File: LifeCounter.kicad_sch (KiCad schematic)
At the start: 0 parts

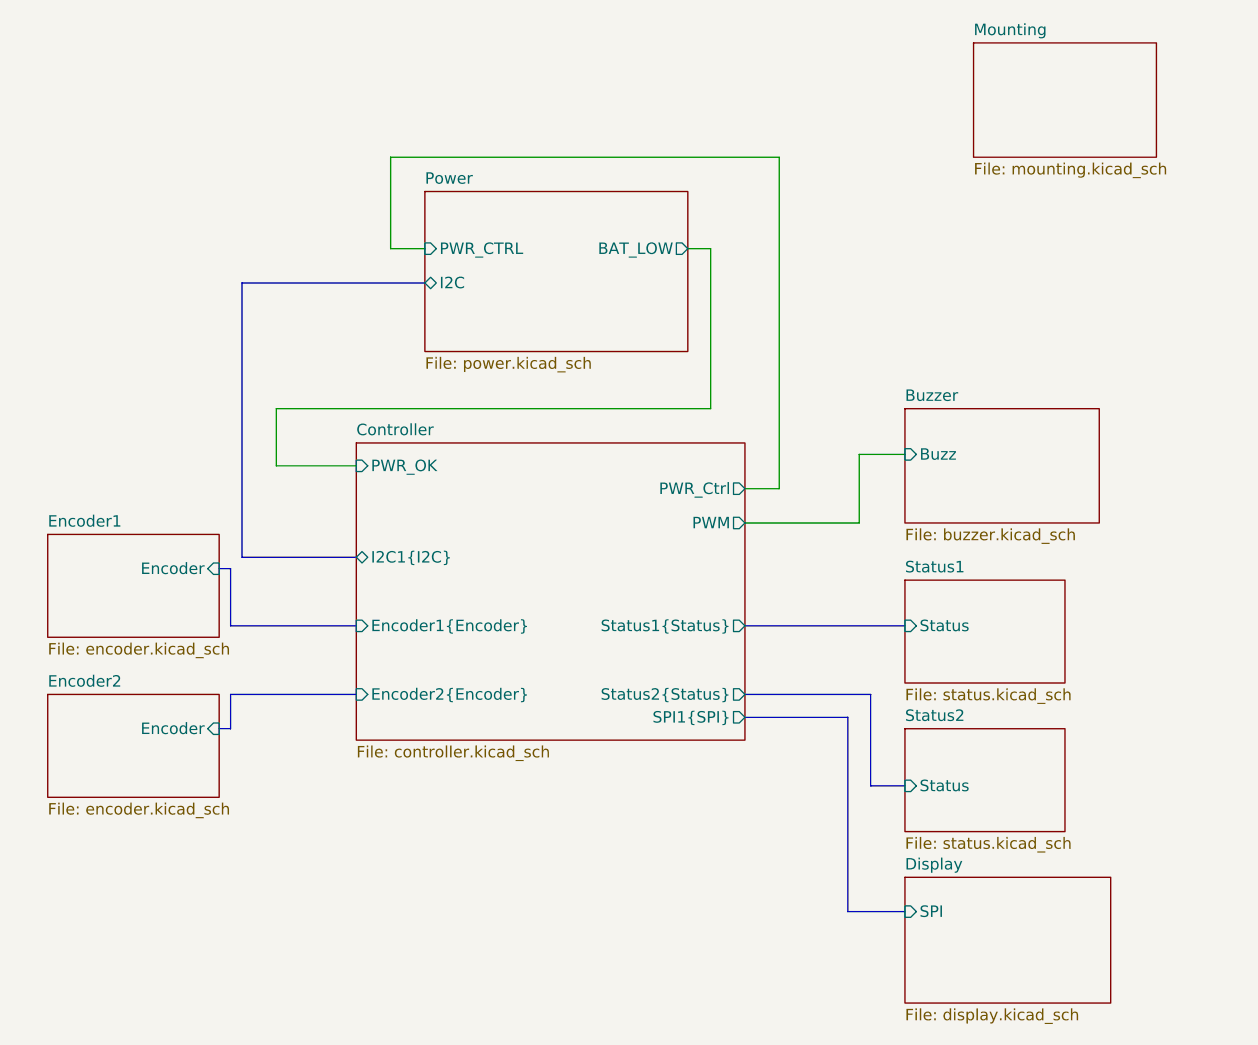
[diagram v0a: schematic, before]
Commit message: Decoupling caps for ICs
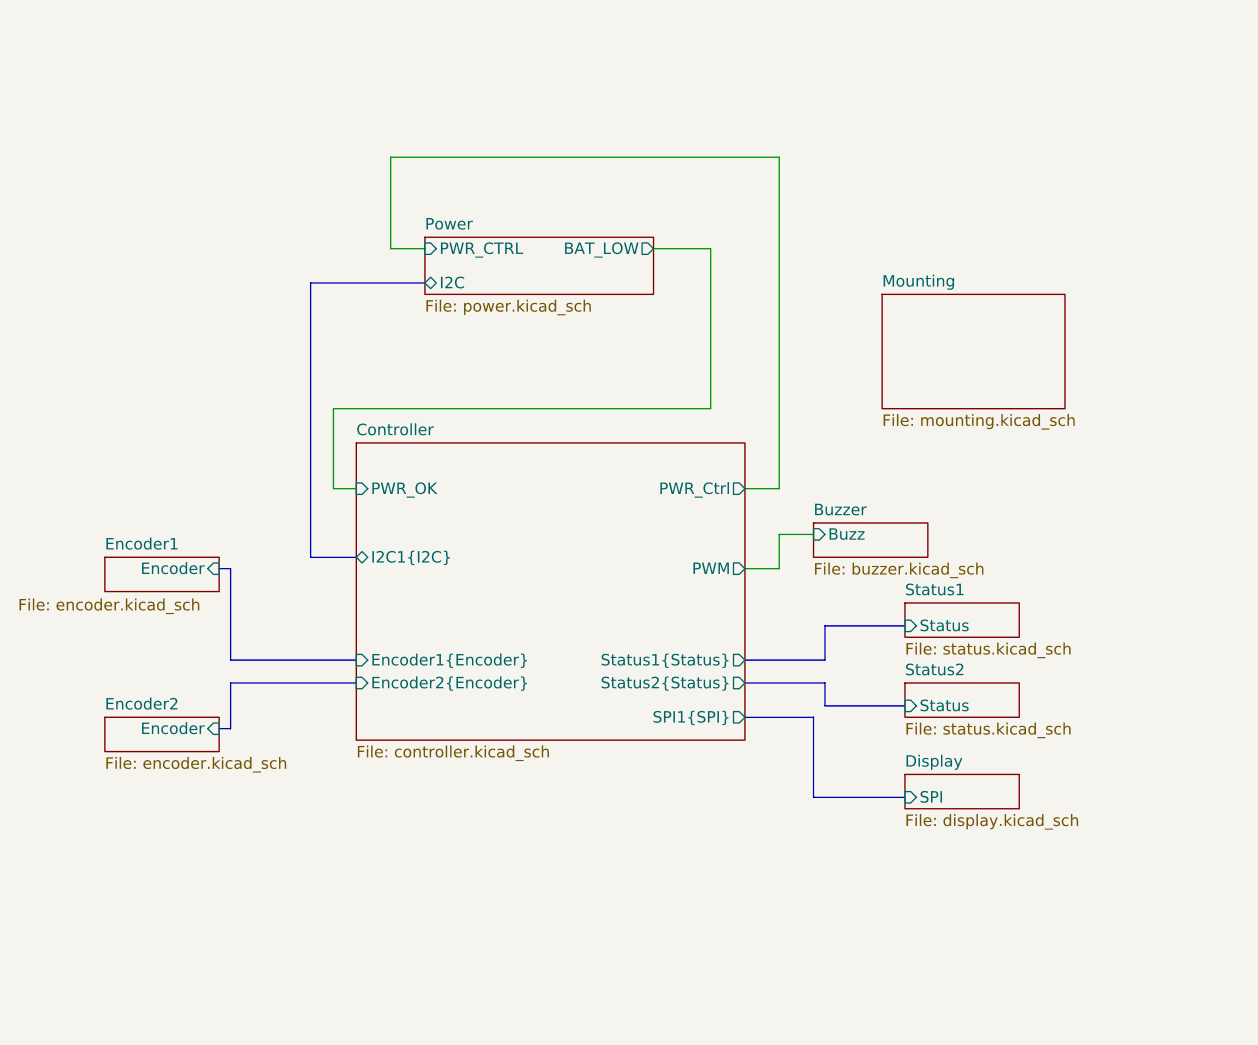
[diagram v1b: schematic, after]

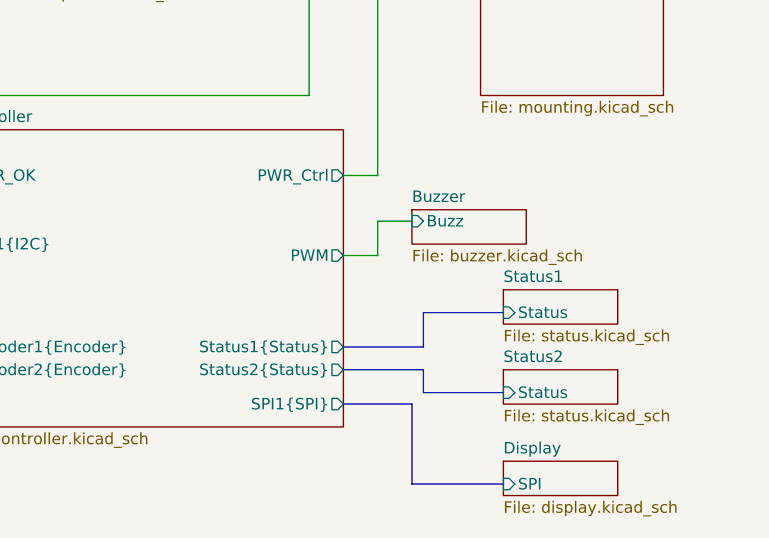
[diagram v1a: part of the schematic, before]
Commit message: Constant current sink to status LEDs and rewiring controller
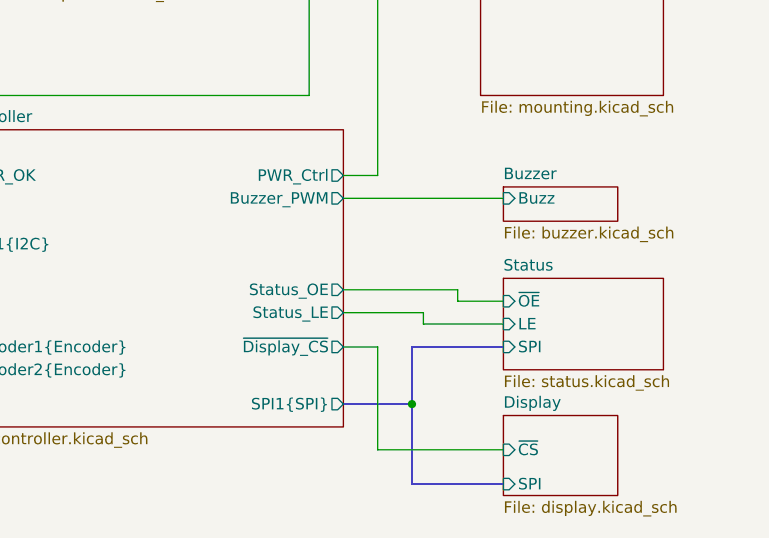
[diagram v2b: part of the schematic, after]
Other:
- sheet Status1 renamed Status
- removed sheet Status2
- sheet Controller ports: added Buzzer_PWM, Status_LE, Status_OE, ~{Display_CS}; removed PWM, Status1{Status}, Status2{Status}
- sheet Display ports: added ~{CS}; removed none
- sheet Status ports: added LE, SPI, ~{OE}; removed Status

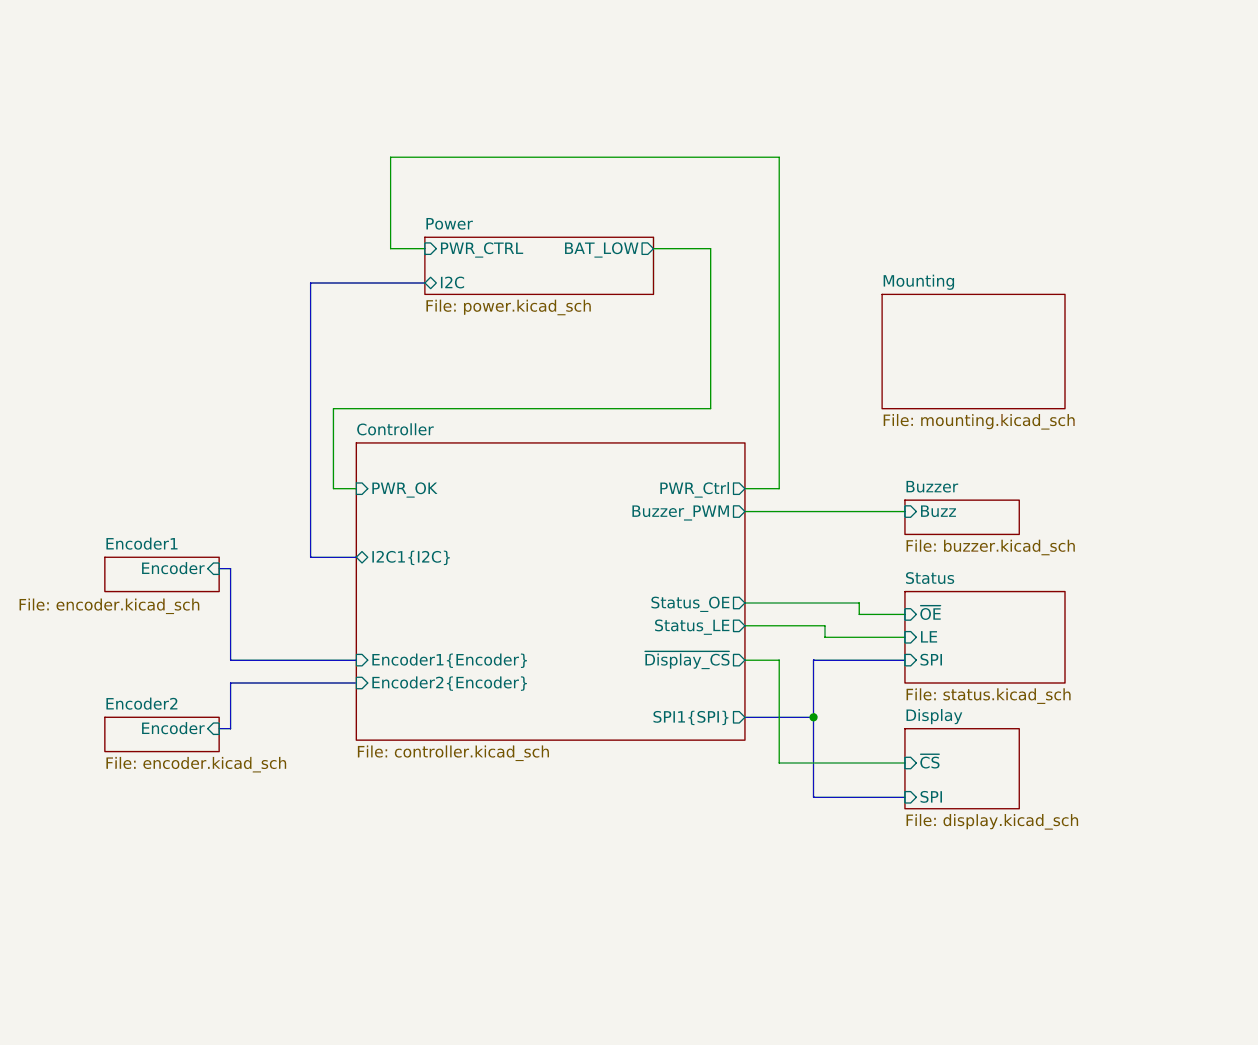
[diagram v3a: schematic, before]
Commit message: Resolve ERC warnings
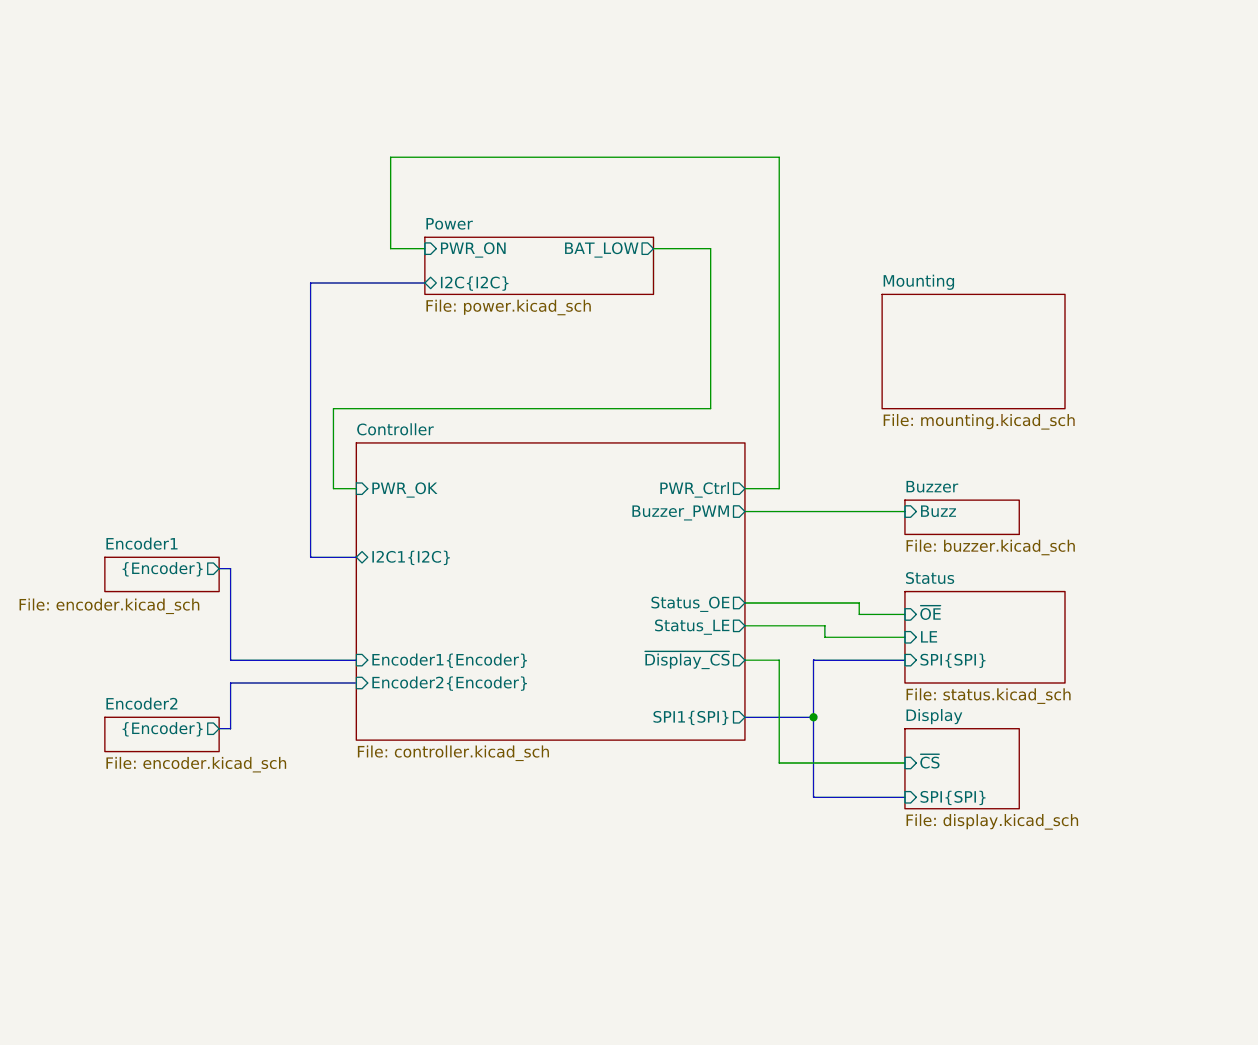
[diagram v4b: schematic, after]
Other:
- sheet Display ports: added SPI{SPI}; removed SPI
- sheet Encoder1 ports: added {Encoder}; removed Encoder
- sheet Encoder2 ports: added {Encoder}; removed Encoder
- sheet Power ports: added I2C{I2C}, PWR_ON; removed I2C, PWR_CTRL
- sheet Status ports: added SPI{SPI}; removed SPI
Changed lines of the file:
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@@
 			)
 		)
-		(pin "SPI" input
+		(pin "SPI{SPI}" input
 			(at 187.96 137.16 180)
 			(effects
@@
 			)
 		)
-		(pin "Encoder" input
+		(pin "{Encoder}" output
 			(at 111.76 129.54 0)
 			(effects
@@
 			)
 		)
-		(pin "SPI" input
+		(pin "SPI{SPI}" input
 			(at 187.96 121.92 180)
 			(effects
@@
 			)
 		)
-		(pin "PWR_CTRL" input
-			(at 134.62 76.2 180)
-			(effects
-				(font
-					(size 1.27 1.27)
-				)
-				(justify left)
-			)
-		)
 		(pin "BAT_LOW" output
 			(at 160.02 76.2 0)
@@
 			)
 		)
-		(pin "I2C" bidirectional
+		(pin "I2C{I2C}" bidirectional
 			(at 134.62 80.01 180)
+			(effects
+				(font
+					(size 1.27 1.27)
+				)
+				(justify left)
+			)
+		)
+		(pin "PWR_ON" input
+			(at 134.62 76.2 180)
 			(effects
 				(font
@@
 			)
 		)
-		(pin "Encoder" input
+		(pin "{Encoder}" output
 			(at 111.76 111.76 0)
 			(effects

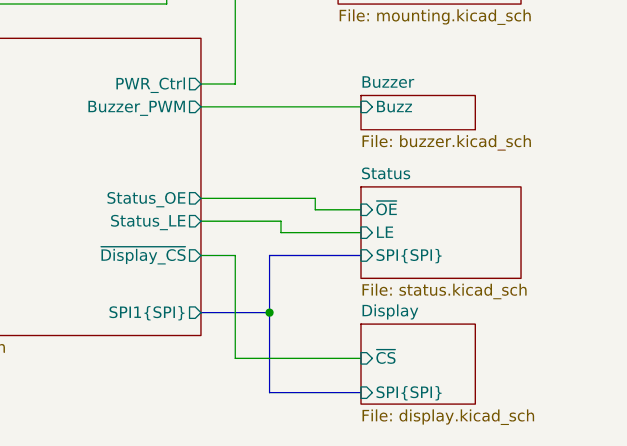
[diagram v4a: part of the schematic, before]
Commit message: Remove display and status for redo
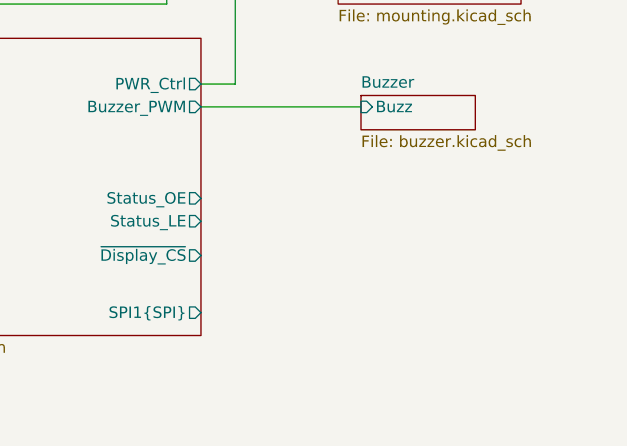
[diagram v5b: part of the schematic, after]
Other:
- removed sheet Display
- removed sheet Status
